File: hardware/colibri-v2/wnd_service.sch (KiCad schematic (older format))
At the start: 31 parts, among them P10 CONN_01X08, P6 CONN_01X08, P7 CONN_01X04, P8 CONN_01X04, P9 CONN_01X04, Q15 BSS138PW, Q16 BSS138PW, SW11 WURTH 436353045816

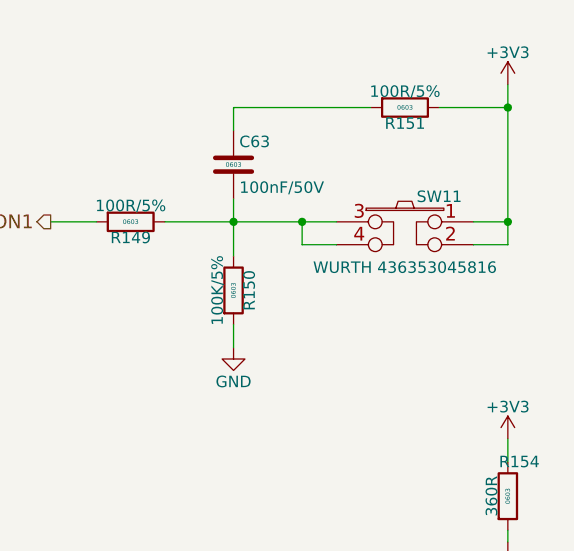
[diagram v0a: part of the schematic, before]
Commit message: Replaced the SDRAM with TFBGA-54
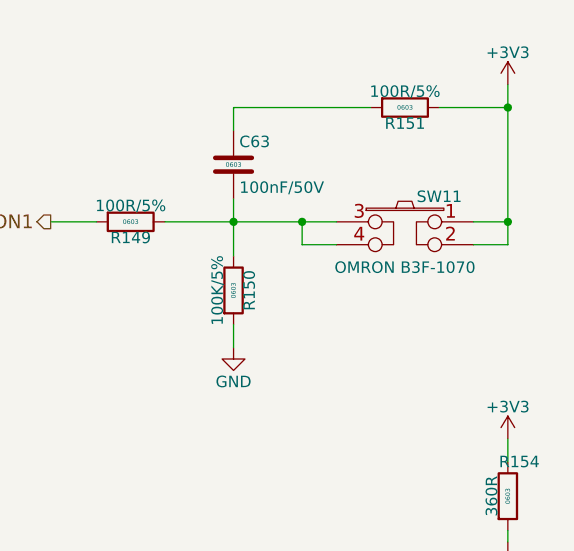
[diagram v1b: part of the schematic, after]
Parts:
- SW11: value WURTH 436353045816 -> OMRON B3F-1070; footprint (none) -> Sigmadrone:SW_TH_Tactile_Omron_B3F-10xx_6x6
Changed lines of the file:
@@
 $Descr A4 11693 8268
 encoding utf-8
-Sheet 21 28
+Sheet 20 28
 Title ""
 Date ""
@@
 F 6 "Farnell" H 8980 1070 30  0001 L CNN "Provider"
 	1    8950 1300
-	1    0    0    -1
-$EndComp
-$Comp
-L SW_PUSH_TACKTILE SW11
-U 1 1 56AAF74F
-P 9700 1550
-F 0 "SW11" H 9850 1660 50  0000 C CNN
-F 1 "WURTH 436353045816" H 9700 1350 50  0000 C CNN
-F 2 "" H 9700 1550 60  0000 C CNN
-F 3 "" H 9700 1550 60  0000 C CNN
-	1    9700 1550
 	1    0    0    -1
 $EndComp
@@
 F 0 "P10" H 1478 6438 50  0000 L CNN
 F 1 "CONN_01X08" H 1478 6346 50  0000 L CNN
-F 2 "" H 1400 6400 50  0000 C CNN
+F 2 "" H 1400 6400 50  0001 C CNN
 F 3 "" H 1400 6400 50  0000 C CNN
 	1    1400 6400
@@
 F 0 "P6" H 1478 1438 50  0000 L CNN
 F 1 "CONN_01X08" H 1478 1346 50  0000 L CNN
-F 2 "" H 1400 1400 50  0000 C CNN
+F 2 "" H 1400 1400 50  0001 C CNN
 F 3 "" H 1400 1400 50  0000 C CNN
 	1    1400 1400
@@
 F 0 "P7" H 1478 2738 50  0000 L CNN
 F 1 "CONN_01X04" H 1478 2646 50  0000 L CNN
-F 2 "" H 1400 2700 50  0000 C CNN
+F 2 "" H 1400 2700 50  0001 C CNN
 F 3 "" H 1400 2700 50  0000 C CNN
 	1    1400 2700
@@
 F 0 "P8" H 1478 3888 50  0000 L CNN
 F 1 "CONN_01X04" H 1478 3796 50  0000 L CNN
-F 2 "" H 1400 3850 50  0000 C CNN
+F 2 "" H 1400 3850 50  0001 C CNN
 F 3 "" H 1400 3850 50  0000 C CNN
 	1    1400 3850
@@
 F 0 "P9" H 1478 5038 50  0000 L CNN
 F 1 "CONN_01X04" H 1478 4946 50  0000 L CNN
-F 2 "" H 1400 5000 50  0000 C CNN
+F 2 "" H 1400 5000 50  0001 C CNN
 F 3 "" H 1400 5000 50  0000 C CNN
 	1    1400 5000
@@
 	1    0    0    -1
 $EndComp
+$Comp
+L SW_PUSH_TACKTILE SW11
+U 1 1 56CC5AF9
+P 9700 1550
+F 0 "SW11" H 9850 1660 50  0000 C CNN
+F 1 "OMRON B3F-1070" H 9700 1350 50  0000 C CNN
+F 2 "Sigmadrone:SW_TH_Tactile_Omron_B3F-10xx_6x6" H 9700 1550 60  0001 C CNN
+F 3 "" H 9700 1550 60  0000 C CNN
+	1    9700 1550
+	1    0    0    -1
+$EndComp

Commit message: Adding and assigning footprints
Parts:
- P10, P6: footprint (none) -> Pin_Headers:Pin_Header_Straight_1x08
- P7, P8, P9: footprint (none) -> Pin_Headers:Pin_Header_Straight_1x04
- Q15, Q16: footprint (none) -> TO_SOT_Packages_SMD:SOT-323
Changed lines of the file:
@@
 F 0 "Q15" H 10350 3700 50  0000 R CNN
 F 1 "BSS138PW" H 10050 3850 50  0000 R CNN
-F 2 "" H 10250 3750 29  0001 C CNN
+F 2 "TO_SOT_Packages_SMD:SOT-323" H 10250 3750 29  0001 C CNN
 F 3 "" H 10050 3650 60  0000 C CNN
 	1    10050 3650
@@
 F 0 "Q16" H 10350 5800 50  0000 R CNN
 F 1 "BSS138PW" H 10050 5950 50  0000 R CNN
-F 2 "" H 10250 5850 29  0001 C CNN
+F 2 "TO_SOT_Packages_SMD:SOT-323" H 10250 5850 29  0001 C CNN
 F 3 "" H 10050 5750 60  0000 C CNN
 	1    10050 5750
@@
 F 0 "P10" H 1478 6438 50  0000 L CNN
 F 1 "CONN_01X08" H 1478 6346 50  0000 L CNN
-F 2 "" H 1400 6400 50  0001 C CNN
+F 2 "Pin_Headers:Pin_Header_Straight_1x08" H 1400 6400 50  0001 C CNN
 F 3 "" H 1400 6400 50  0000 C CNN
 	1    1400 6400
@@
 F 0 "P6" H 1478 1438 50  0000 L CNN
 F 1 "CONN_01X08" H 1478 1346 50  0000 L CNN
-F 2 "" H 1400 1400 50  0001 C CNN
+F 2 "Pin_Headers:Pin_Header_Straight_1x08" H 1400 1400 50  0001 C CNN
 F 3 "" H 1400 1400 50  0000 C CNN
 	1    1400 1400
@@
 F 0 "P7" H 1478 2738 50  0000 L CNN
 F 1 "CONN_01X04" H 1478 2646 50  0000 L CNN
-F 2 "" H 1400 2700 50  0001 C CNN
+F 2 "Pin_Headers:Pin_Header_Straight_1x04" H 1400 2700 50  0001 C CNN
 F 3 "" H 1400 2700 50  0000 C CNN
 	1    1400 2700
@@
 F 0 "P8" H 1478 3888 50  0000 L CNN
 F 1 "CONN_01X04" H 1478 3796 50  0000 L CNN
-F 2 "" H 1400 3850 50  0001 C CNN
+F 2 "Pin_Headers:Pin_Header_Straight_1x04" H 1400 3850 50  0001 C CNN
 F 3 "" H 1400 3850 50  0000 C CNN
 	1    1400 3850
@@
 F 0 "P9" H 1478 5038 50  0000 L CNN
 F 1 "CONN_01X04" H 1478 4946 50  0000 L CNN
-F 2 "" H 1400 5000 50  0001 C CNN
+F 2 "Pin_Headers:Pin_Header_Straight_1x04" H 1400 5000 50  0001 C CNN
 F 3 "" H 1400 5000 50  0000 C CNN
 	1    1400 5000

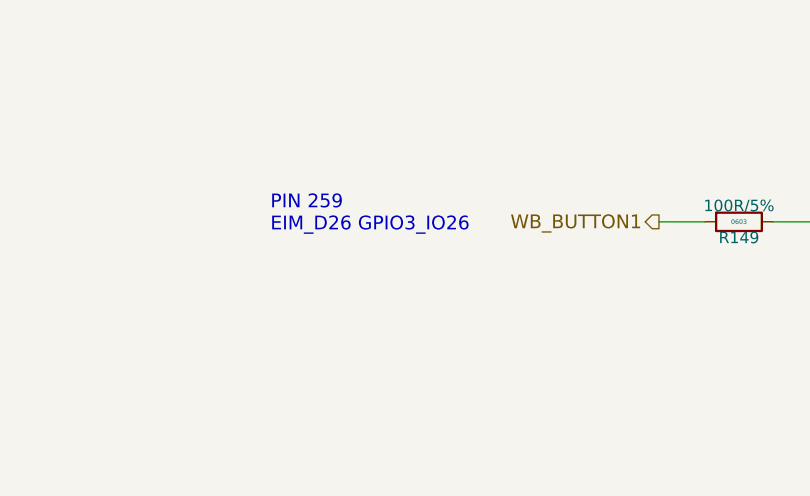
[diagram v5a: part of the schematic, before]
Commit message: Added SPPJ320600.kicad_mod
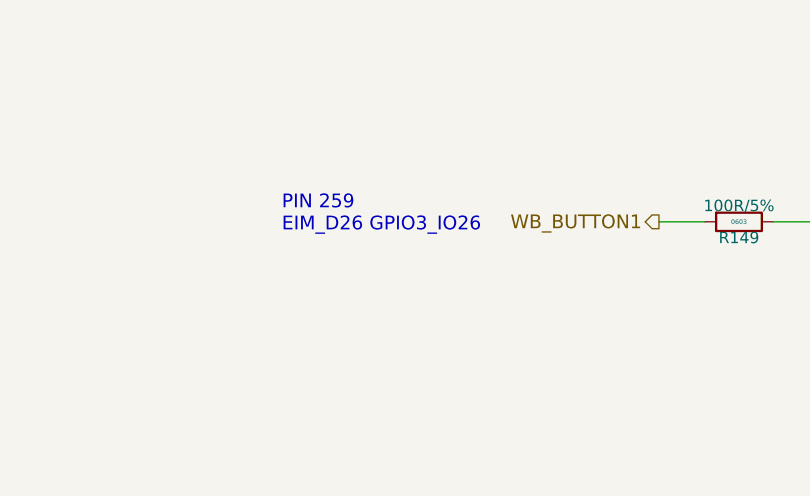
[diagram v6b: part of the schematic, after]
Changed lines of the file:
@@
 Text Notes 7600 3700 0    60   ~ 0
 PIN 261\nEIM_DA8 GPIO3_IO08
-Text Notes 6450 1600 0    60   ~ 0
+Text Notes 6500 1600 0    60   ~ 0
 PIN 259\nEIM_D26 GPIO3_IO26
 $Comp

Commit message: Added AP6681GMT-HF-3.kicad_mod. Fixed netlist errors
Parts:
- DL11, DL12: footprint LEDs:LED-0603 -> LEDs:LED_0603
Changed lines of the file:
@@
 F 0 "DL11" H 10150 3250 50  0000 C CNN
 F 1 "GREEN" H 10150 3050 50  0000 C CNN
-F 2 "LEDs:LED-0603" H 10150 3000 30  0001 C CNN
+F 2 "LEDs:LED_0603" H 10150 3000 30  0001 C CNN
 F 3 "" H 10150 3150 60  0000 C CNN
 F 4 "0603" H 10035 3130 30  0000 C CNN "SMT"
@@
 F 0 "DL12" V 10250 5150 50  0000 C CNN
 F 1 "RED" H 10100 5350 50  0000 C CNN
-F 2 "LEDs:LED-0603" H 10150 5100 30  0001 C CNN
+F 2 "LEDs:LED_0603" H 10150 5100 30  0001 C CNN
 F 3 "" H 10150 5250 60  0000 C CNN
 F 4 "0603" H 10035 5230 30  0000 C CNN "SMT"
